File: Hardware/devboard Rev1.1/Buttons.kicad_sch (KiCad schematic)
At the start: 15 parts, among them SW4 LEFT, SW5 UP, SW6 ENTER, SW7 DOWN, SW8 RIGHT

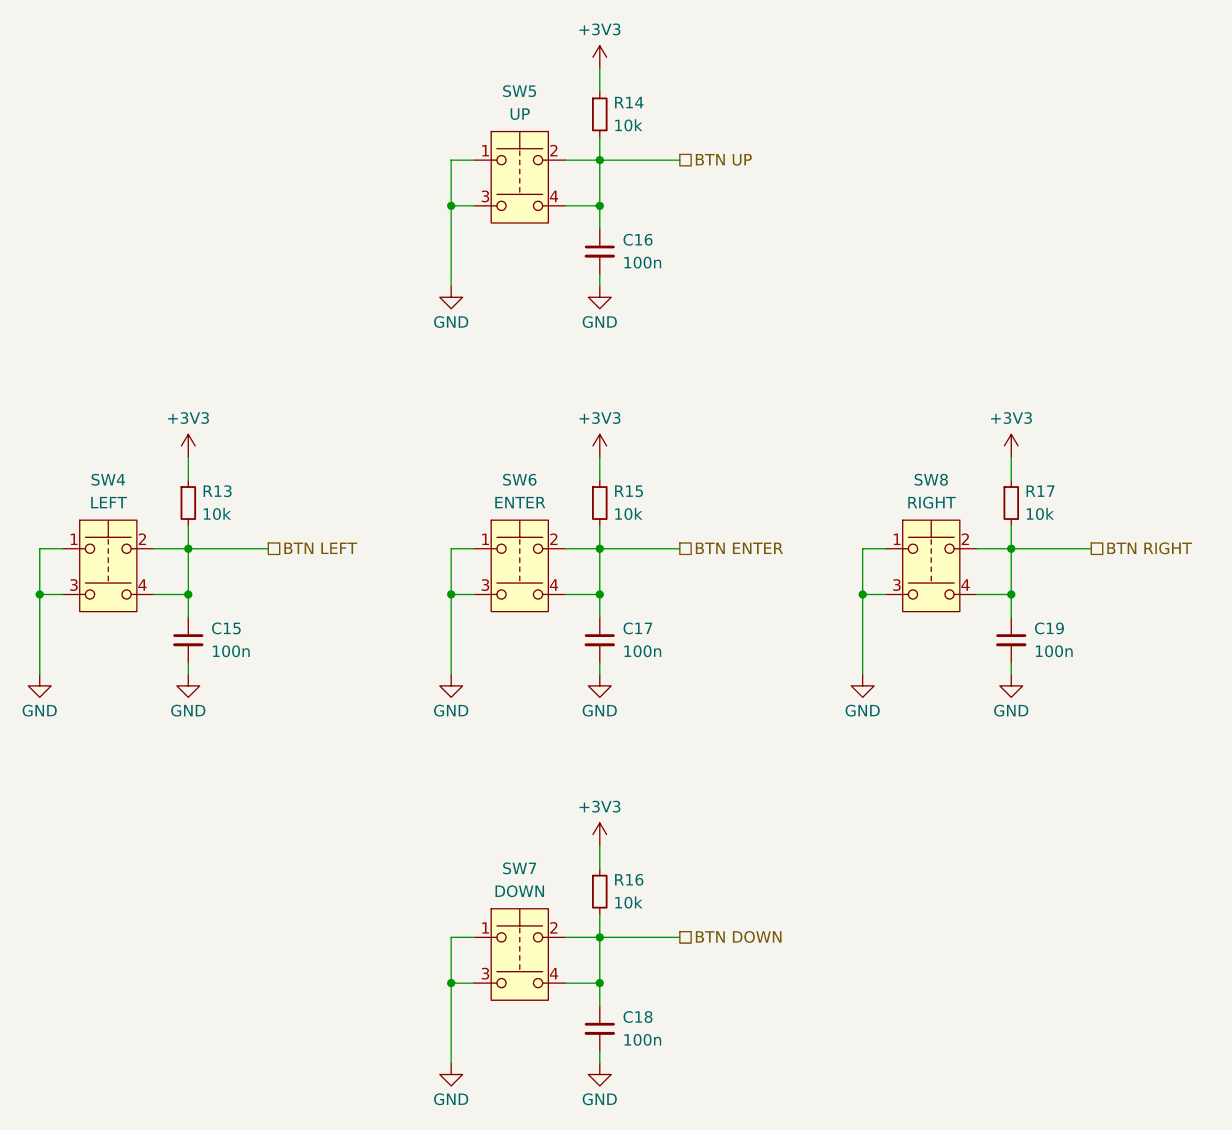
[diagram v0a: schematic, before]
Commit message: fixed switch footprint and changed buttons pins to avoid bootstrapping pins
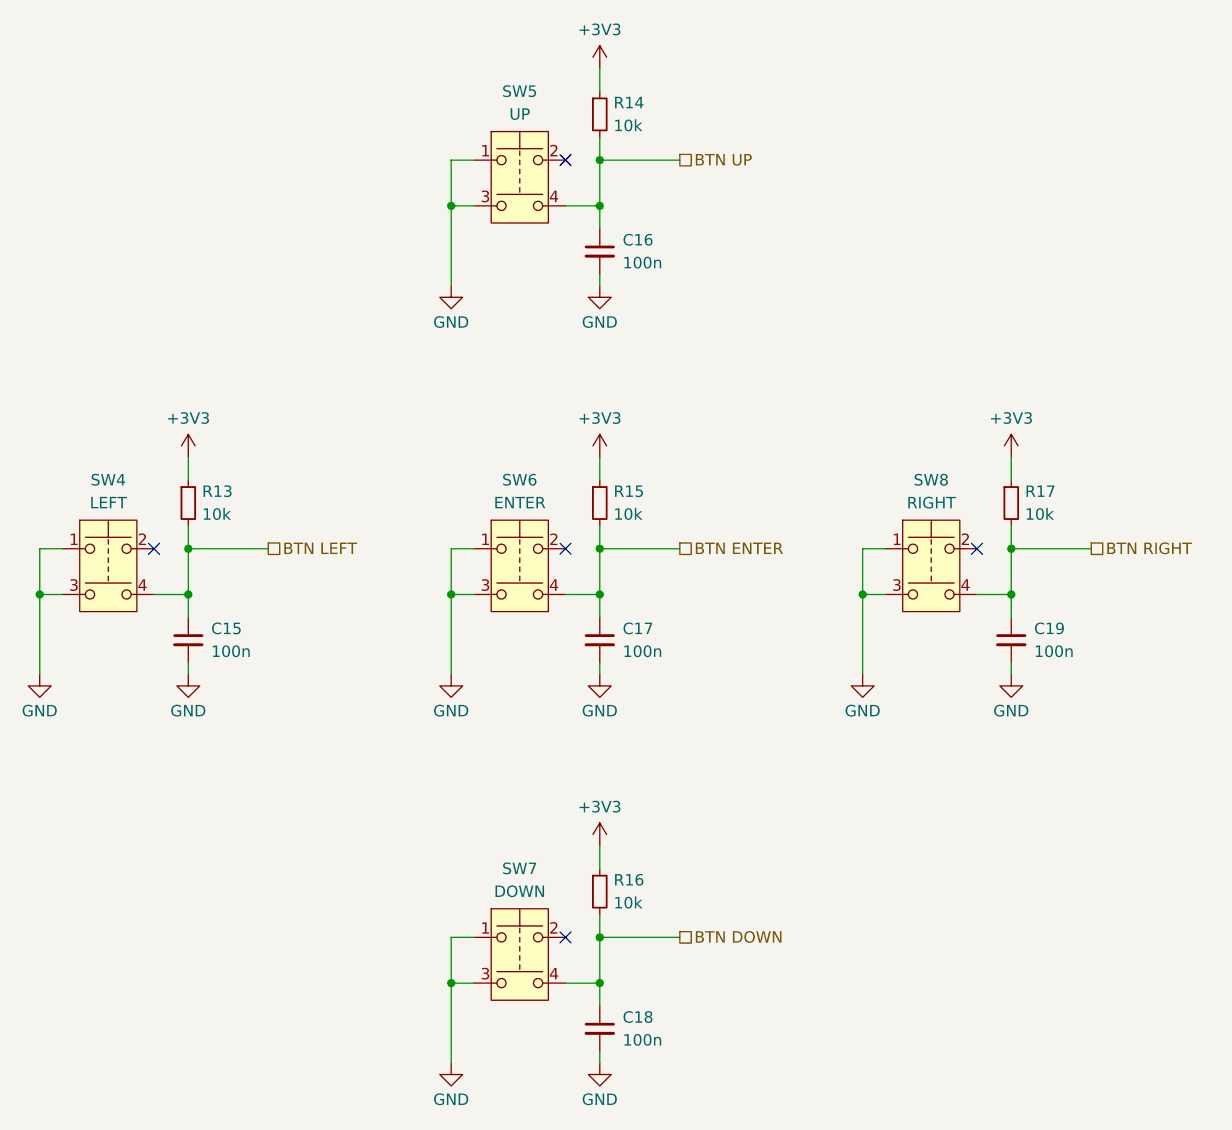
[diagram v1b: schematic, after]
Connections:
- net BTN DOWN: no longer SW7.2
- net BTN ENTER: no longer SW6.2
- net BTN LEFT: no longer SW4.2
- net BTN RIGHT: no longer SW8.2
- net BTN UP: no longer SW5.2
- no-connect marks 0 -> 5
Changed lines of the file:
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@@
 		(color 0 0 0 0)
 	)
+	(no_connect
+		(at 106.68 92.71)
+	)
+	(no_connect
+		(at 152.4 49.53)
+	)
+	(no_connect
+		(at 152.4 92.71)
+	)
+	(no_connect
+		(at 152.4 135.89)
+	)
+	(no_connect
+		(at 198.12 92.71)
+	)
 	(wire
 		(pts
@@
 	(wire
 		(pts
-			(xy 152.4 135.89) (xy 156.21 135.89)
-		)
-		(stroke
-			(width 0)
-			(type default)
-		)
-	)
-	(wire
-		(pts
 			(xy 156.21 135.89) (xy 156.21 133.35)
 		)
@@
 	(wire
 		(pts
-			(xy 152.4 49.53) (xy 156.21 49.53)
-		)
-		(stroke
-			(width 0)
-			(type default)
-		)
-	)
-	(wire
-		(pts
 			(xy 139.7 140.97) (xy 139.7 149.86)
 		)
@@
 	(wire
 		(pts
-			(xy 152.4 92.71) (xy 156.21 92.71)
-		)
-		(stroke
-			(width 0)
-			(type default)
-		)
-	)
-	(wire
-		(pts
 			(xy 201.93 92.71) (xy 210.82 92.71)
 		)
@@
 	(wire
 		(pts
-			(xy 106.68 92.71) (xy 110.49 92.71)
-		)
-		(stroke
-			(width 0)
-			(type default)
-		)
-	)
-	(wire
-		(pts
 			(xy 110.49 106.68) (xy 110.49 105.41)
 		)
@@
 		)
 		(stroke
-			(width 0)
-			(type default)
-		)
-	)
-	(wire
-		(pts
-			(xy 198.12 92.71) (xy 201.93 92.71)
-		)
-		(stroke
